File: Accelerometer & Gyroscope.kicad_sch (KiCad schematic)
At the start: 5 parts, among them U9 LSM6DS3

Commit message: Restructuring
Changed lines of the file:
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@@
 	(title_block
 		(title "3D Accelerometer & 3D Gyroscope")
-		(date "2026-01-23")
+		(date "2026-01-25")
 		(rev "v0.0")
 		(company "TJ71PL")
@@
 		)
 	)
-	(hierarchical_label "AG{INT, SCL, SDA}"
+	(hierarchical_label "AG{SDA, SCL, INT}"
 		(shape bidirectional)
 		(at 191.77 101.6 0)
@@
 		)
 	)
-	(hierarchical_label "AG{INT, SCL, SDA}"
+	(hierarchical_label "AG{SDA, SCL, INT}"
 		(shape bidirectional)
 		(at 97.79 93.98 180)

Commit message: Pin out completion
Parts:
- removed R19, R20: 10K, Resistor_SMD:R_0402_1005Metric, symbol Device:R
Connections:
- net +3V0 is gone; now on net +3.3V: C38.1, C39.1, U9.5 (VDDIO), U9.8 (VDD)

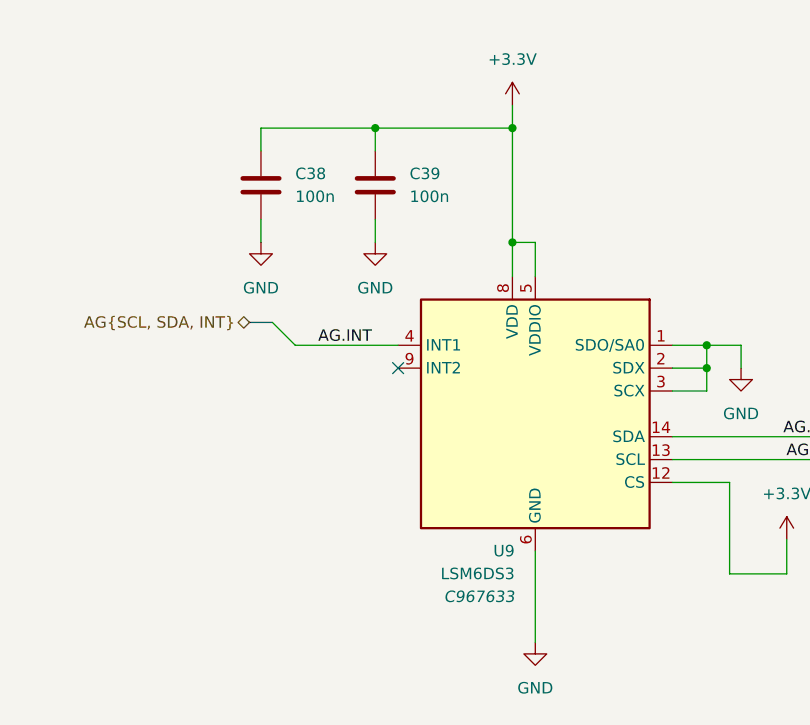
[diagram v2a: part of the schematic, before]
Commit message: Removal of Colon LEDs
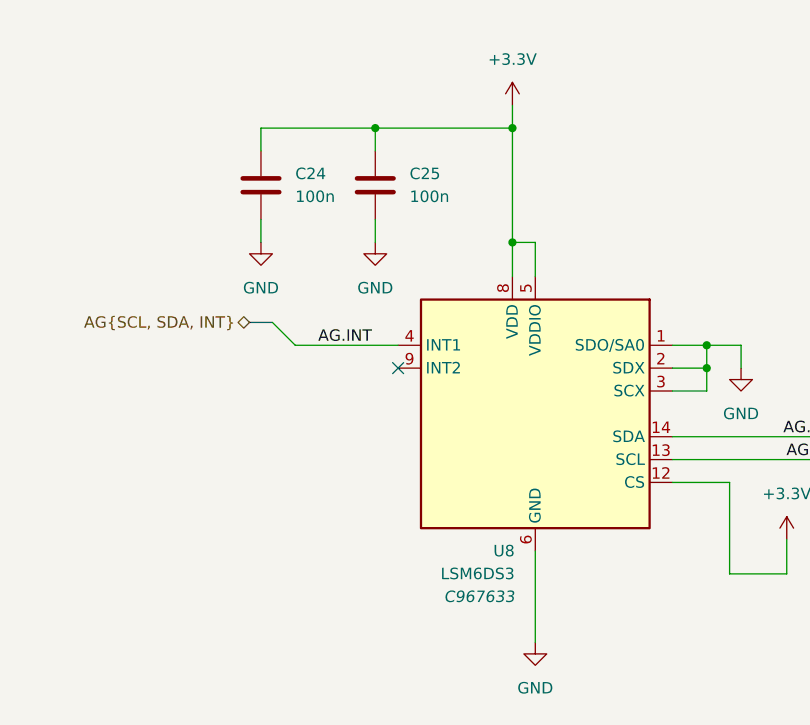
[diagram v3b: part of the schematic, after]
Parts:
- renumbered C38 to C24, C39 to C25, U9 to U8
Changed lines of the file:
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@@
 		(dnp no)
 		(fields_autoplaced yes)
-		(property "Reference" "#PWR054"
+		(property "Reference" "#PWR061"
 			(at 128.27 73.66 0)
 			(effects
@@
 			(project "Precision Clock"
 				(path "/c9a8ff63-a0d1-4125-9dd1-40fb53daf536/83e9a93f-b32e-4175-81a6-6f58261db903"
-					(reference "#PWR054")
+					(reference "#PWR061")
 					(unit 1)
 				)
@@
 		(on_board yes)
 		(dnp no)
-		(property "Reference" "U9"
+		(property "Reference" "U8"
 			(at 128.524 119.38 0)
 			(effects
@@
 			(project "Precision Clock"
 				(path "/c9a8ff63-a0d1-4125-9dd1-40fb53daf536/83e9a93f-b32e-4175-81a6-6f58261db903"
-					(reference "U9")
+					(reference "U8")
 					(unit 1)
 				)
@@
 		(dnp no)
 		(fields_autoplaced yes)
-		(property "Reference" "C39"
+		(property "Reference" "C25"
 			(at 116.84 77.4699 0)
 			(effects
@@
 			(project "Precision Clock"
 				(path "/c9a8ff63-a0d1-4125-9dd1-40fb53daf536/83e9a93f-b32e-4175-81a6-6f58261db903"
-					(reference "C39")
+					(reference "C25")
 					(unit 1)
 				)
@@
 		(dnp no)
 		(fields_autoplaced yes)
-		(property "Reference" "#PWR069"
+		(property "Reference" "#PWR060"
 			(at 113.03 91.44 0)
 			(effects
@@
 			(project "Precision Clock"
 				(path "/c9a8ff63-a0d1-4125-9dd1-40fb53daf536/83e9a93f-b32e-4175-81a6-6f58261db903"
-					(reference "#PWR069")
+					(reference "#PWR060")
 					(unit 1)
 				)
@@
 		(dnp no)
 		(fields_autoplaced yes)
-		(property "Reference" "#PWR073"
+		(property "Reference" "#PWR064"
 			(at 158.75 121.92 0)
 			(effects
@@
 			(project "Precision Clock"
 				(path "/c9a8ff63-a0d1-4125-9dd1-40fb53daf536/83e9a93f-b32e-4175-81a6-6f58261db903"
-					(reference "#PWR073")
+					(reference "#PWR064")
 					(unit 1)
 				)
@@
 		(dnp no)
 		(fields_autoplaced yes)
-		(property "Reference" "C38"
+		(property "Reference" "C24"
 			(at 104.14 77.4699 0)
 			(effects
@@
 			(project "Precision Clock"
 				(path "/c9a8ff63-a0d1-4125-9dd1-40fb53daf536/83e9a93f-b32e-4175-81a6-6f58261db903"
-					(reference "C38")
+					(reference "C24")
 					(unit 1)
 				)
@@
 		(dnp no)
 		(fields_autoplaced yes)
-		(property "Reference" "#PWR068"
+		(property "Reference" "#PWR059"
 			(at 100.33 91.44 0)
 			(effects
@@
 			(project "Precision Clock"
 				(path "/c9a8ff63-a0d1-4125-9dd1-40fb53daf536/83e9a93f-b32e-4175-81a6-6f58261db903"
-					(reference "#PWR068")
+					(reference "#PWR059")
 					(unit 1)
 				)
@@
 		(dnp no)
 		(fields_autoplaced yes)
-		(property "Reference" "#PWR071"
+		(property "Reference" "#PWR062"
 			(at 130.81 135.89 0)
 			(effects
@@
 			(project "Precision Clock"
 				(path "/c9a8ff63-a0d1-4125-9dd1-40fb53daf536/83e9a93f-b32e-4175-81a6-6f58261db903"
-					(reference "#PWR071")
+					(reference "#PWR062")
 					(unit 1)
 				)
@@
 		(dnp no)
 		(fields_autoplaced yes)
-		(property "Reference" "#PWR072"
+		(property "Reference" "#PWR063"
 			(at 153.67 105.41 0)
 			(effects
@@
 			(project "Precision Clock"
 				(path "/c9a8ff63-a0d1-4125-9dd1-40fb53daf536/83e9a93f-b32e-4175-81a6-6f58261db903"
-					(reference "#PWR072")
-					(unit 1)
-				)
+					(reference "#PWR063")
+					(unit 1)
+				)
